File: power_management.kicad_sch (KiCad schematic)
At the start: 23 parts, among them J3 Conn_01x03_Socket, J8 Conn_01x04_Socket, Q1 Q_NMOS_DGS, Q2 Q_NMOS_DGS, U2 TLV803EA24DCKR, U3 TPS22860, U4 TPS22860, U5 SN74AUP1G74

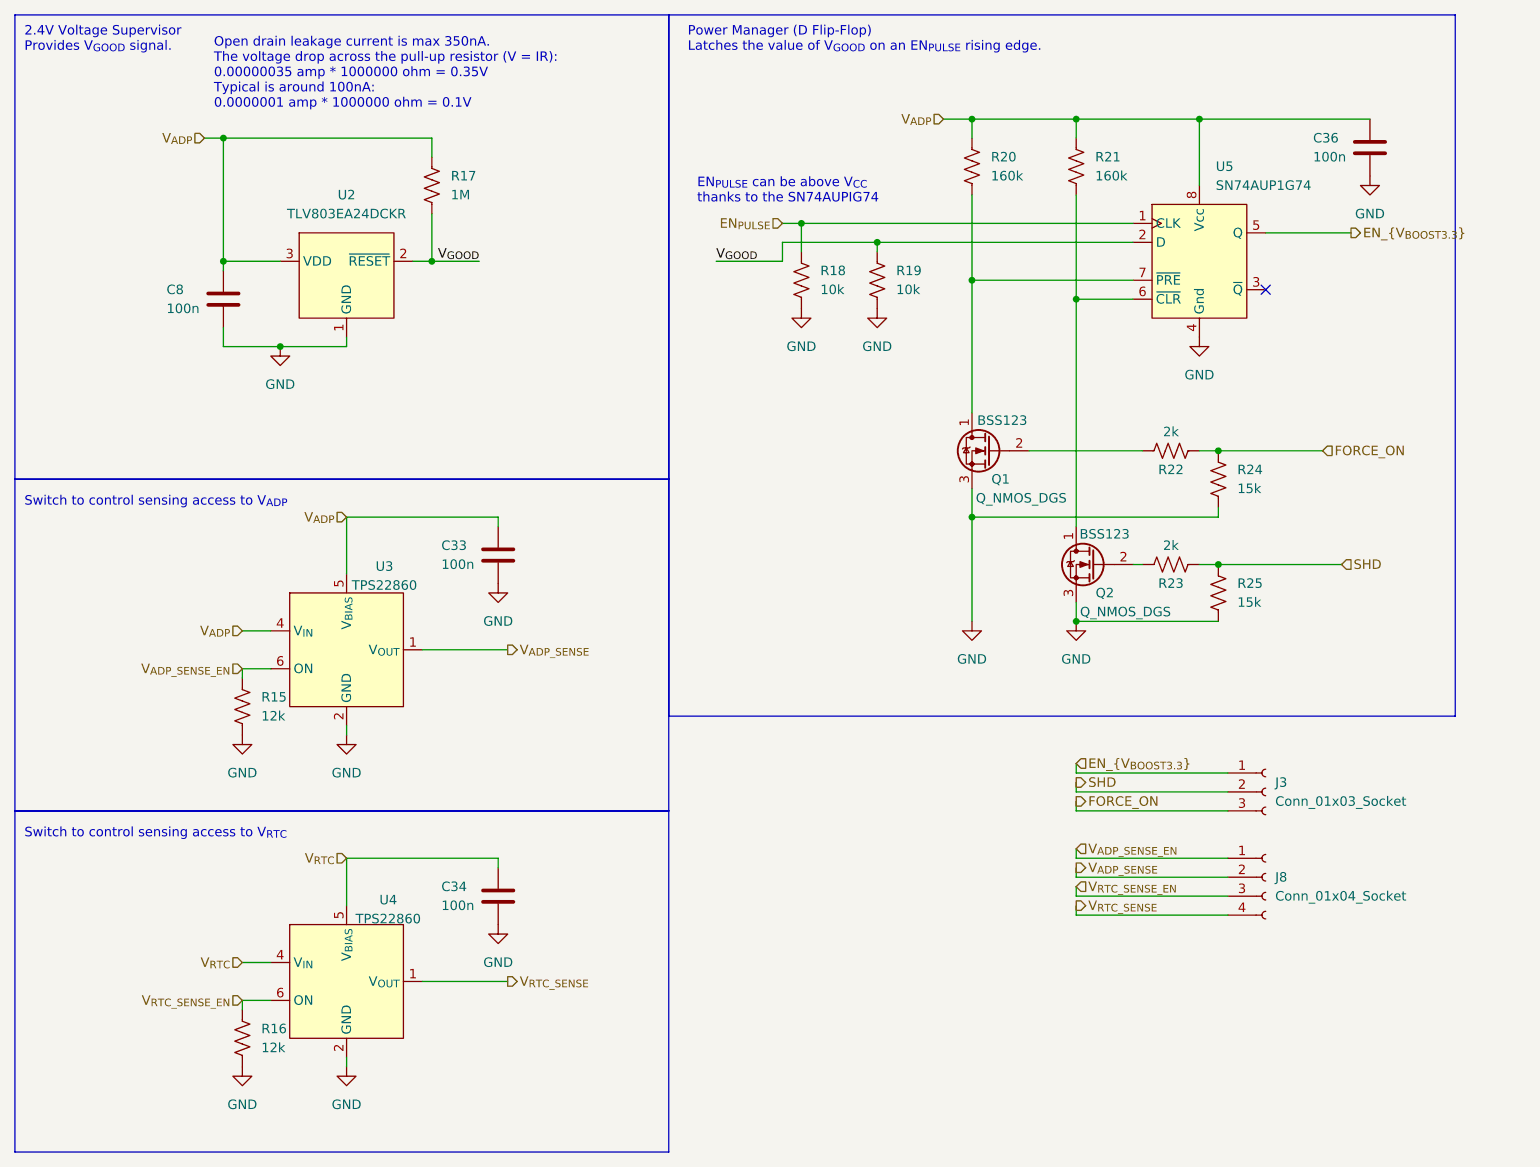
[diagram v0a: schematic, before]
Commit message: Add more informative text, crystal to SMD, headers
 - Added a lot more to the silkscreen to segment parts of the board
 - Changed the 32kHz crystals to an SMD part
 - Added some headers for ADP5091 function
 - Some BOM consolidation, mostly of resistors and capacitors
 - Marked one capacitor as C0G rating
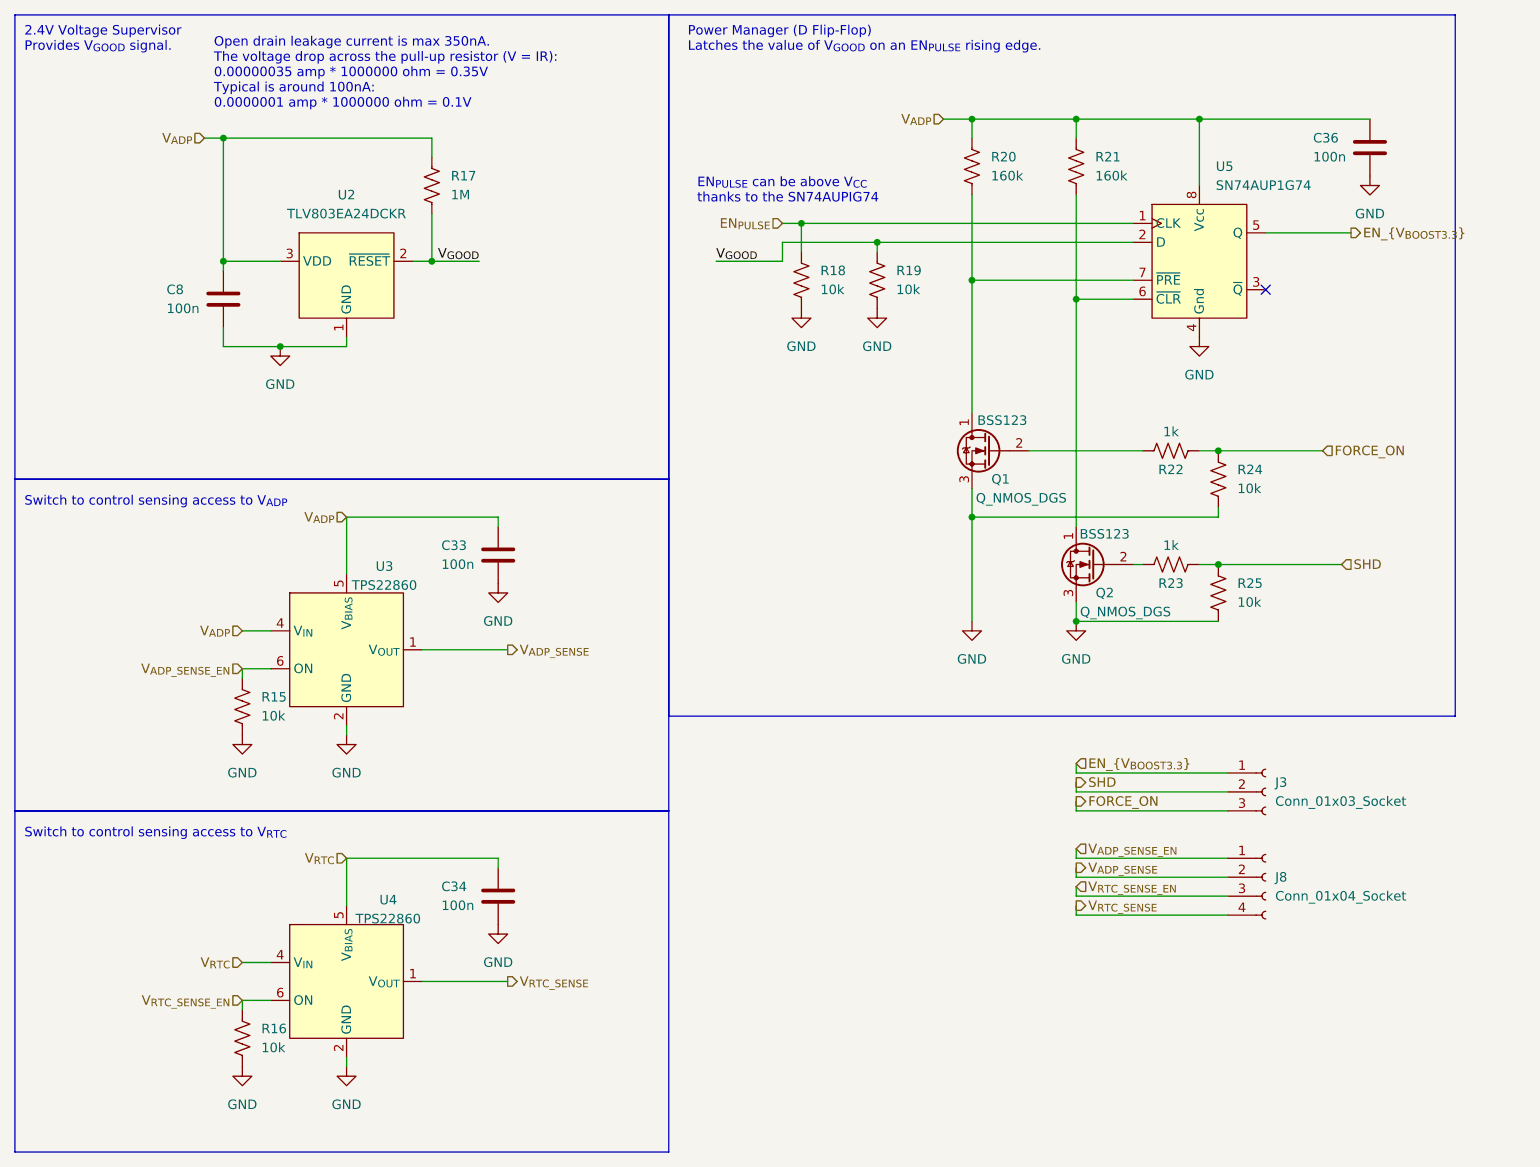
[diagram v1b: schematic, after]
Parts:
- R15, R16: value 12k -> 10k
- R22, R23: value 2k -> 1k
- R24, R25: value 15k -> 10k
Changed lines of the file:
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@@
 			)
 		)
-		(property "Value" "15k"
+		(property "Value" "10k"
 			(at 219.71 96.52 0)
 			(effects
@@
 			)
 		)
-		(property "Value" "12k"
+		(property "Value" "10k"
 			(at 88.9 171.45 0)
 			(effects
@@
 			)
 		)
-		(property "Value" "2k"
+		(property "Value" "1k"
 			(at 210.82 104.14 90)
 			(effects
@@
 			)
 		)
-		(property "Value" "12k"
+		(property "Value" "10k"
 			(at 88.9 127 0)
 			(effects
@@
 			)
 		)
-		(property "Value" "15k"
+		(property "Value" "10k"
 			(at 219.71 111.76 0)
 			(effects
@@
 			)
 		)
-		(property "Value" "2k"
+		(property "Value" "1k"
 			(at 210.82 88.9 90)
 			(effects

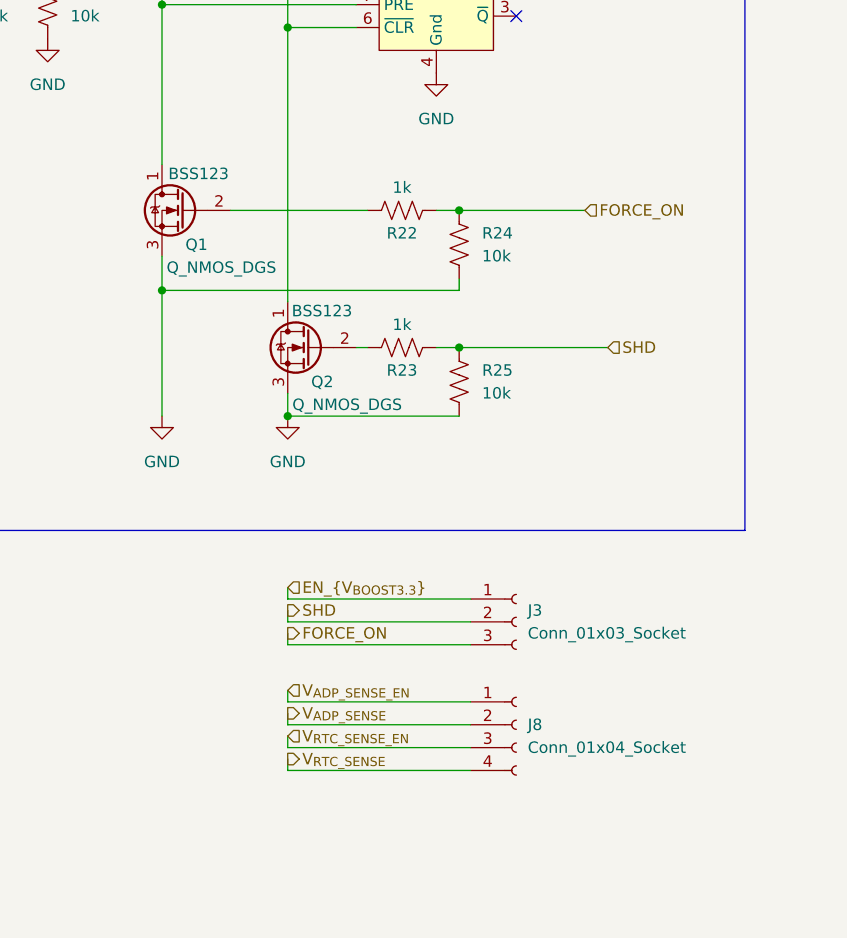
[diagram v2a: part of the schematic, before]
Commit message: Update datasheet and MPN for C and R
 - Update pin headers from sockets to pins
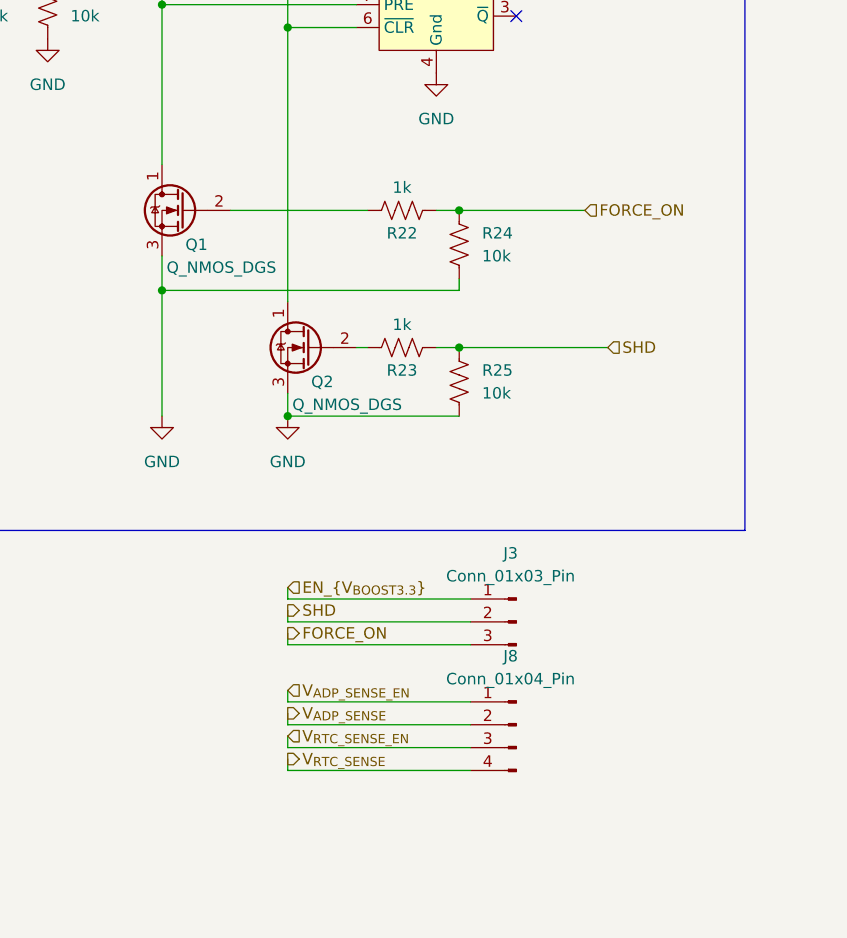
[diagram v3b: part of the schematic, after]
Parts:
- C33, C34, C36, C8: Digikey Product Number (none) -> 1276-1935-2-ND; Manufacturer Product Number (none) -> CL10B104KB8NNWC
- J3: value Conn_01x03_Socket -> Conn_01x03_Pin; symbol Connector:Conn_01x03_Socket -> Connector:Conn_01x03_Pin
- J8: value Conn_01x04_Socket -> Conn_01x04_Pin; symbol Connector:Conn_01x04_Socket -> Connector:Conn_01x04_Pin
- R15, R16, R18, R19, R24, R25: Digikey Product Number (none) -> RMCF0603FT10K0TR-ND; Manufacturer Product Number (none) -> RMCF0603FT10K0
- R17: Digikey Product Number (none) -> 1292-WR06X1004FTLTR-ND; Manufacturer Product Number (none) -> WR06X1004FTL
- R20, R21: Digikey Product Number (none) -> RMCF0603FT160KTR-ND; Manufacturer Product Number (none) -> RMCF0603FT160K
- R22, R23: Digikey Product Number (none) -> RMCF0603FT1K00TR-ND; Manufacturer Product Number (none) -> RMCF0603FT1K00

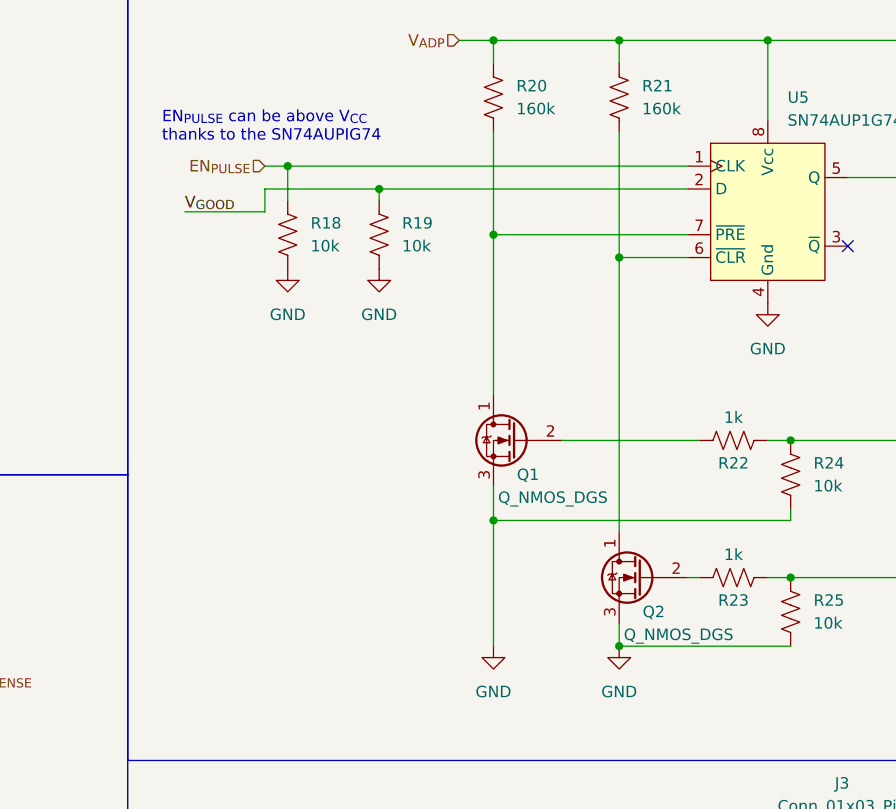
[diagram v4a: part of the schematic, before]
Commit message: Fix BSS123 pins, remove R18 R19 pulldowns
 - BSS123 pinout were completely wrong due to using the wrong symbol in
   the schematic. Made a new symbol with the right pinout. Fixes #7.
 - R18 and R19 were forming a voltage divider as V_GOOD and EN_PULSE
   are open-drain lines. Remove the pull-downs, and pray that circuit
   initialization is sane. Fixes #6.
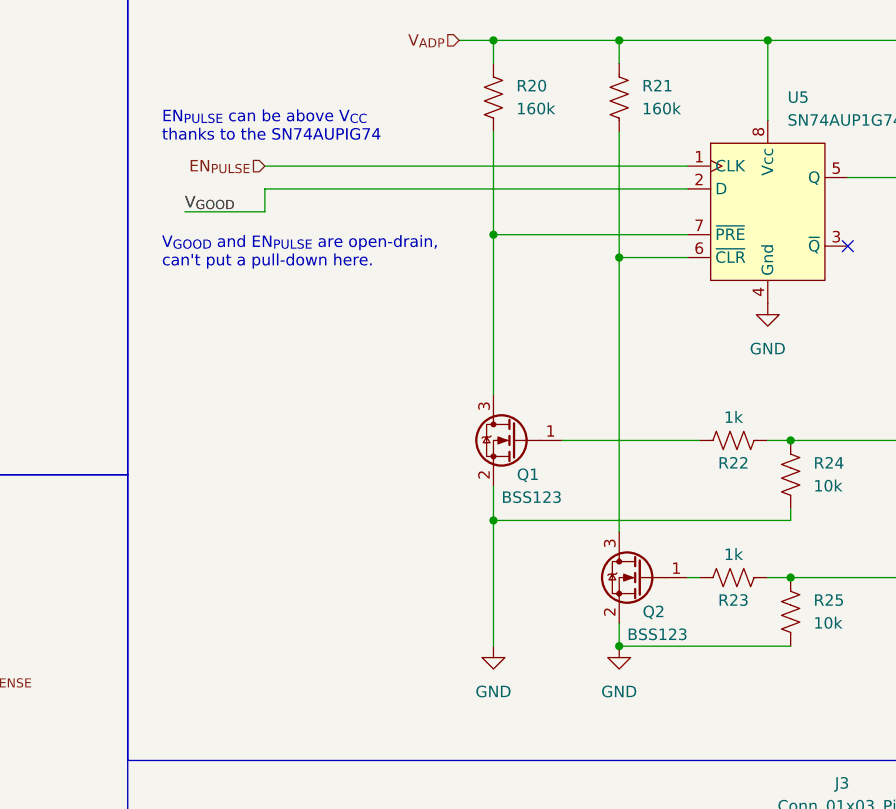
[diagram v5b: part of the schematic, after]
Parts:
- removed R18, R19: 10k, Resistor_SMD:R_0603_1608Metric_Pad0.98x0.95mm_HandSolder, symbol Device:R_US
- Q1, Q2: value Q_NMOS_DGS -> BSS123; footprint Package_TO_SOT_SMD:SOT-23_Handsoldering -> Package_TO_SOT_SMD:SOT-23; symbol Device:Q_NMOS_DGS -> Transistor_FET:BSS123
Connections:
- net GND: now also Q1.2 (S), Q2.2 (S); no longer Q1.3 (S), Q2.3 (S)
- net at R21.2, U5.6 (~{CLR}): now also Q2.3 (D); no longer Q2.1 (D)
- net at R23.1: now also Q2.1 (G); no longer Q2.2 (G)
- net at R20.2, U5.7 (~{PRE}): now also Q1.3 (D); no longer Q1.1 (D)
- net at R22.1: now also Q1.1 (G); no longer Q1.2 (G)
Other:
- note added: "V_{GOOD} and EN_{PULSE} are open-drain, can't put a pull-down here."
